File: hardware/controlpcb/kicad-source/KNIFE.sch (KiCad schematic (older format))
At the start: 13 parts, among them P4 WR-TBL_691313710002, U15 74xx08, U16 IFX007T

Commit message: added kicad source
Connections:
- net +3V3: no longer R42.2
- net IS2 renamed KNIFE_IS
- net KNIFE renamed KNIFE_PWM
- new net KNIFE_INH: R42.2
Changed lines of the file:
@@
 IN_KNIFE
-$Comp
-L power-supply:+3V3 #PWR074
-U 1 1 5ECFE999
-P 1900 2000
-F 0 "#PWR074" H 1900 1850 50  0001 C CNN
-F 1 "+3V3" H 1915 2173 50  0000 C CNN
-F 2 "" H 1900 2000 50  0000 C CNN
-F 3 "" H 1900 2000 50  0000 C CNN
-	1    1900 2000
-	1    0    0    -1
-$EndComp
-Wire Wire Line
-	1900 2050 1900 2000
 $Comp
 L IC_logic:74xx08 U15
@@
 EM_STOP
 Text GLabel 2200 4600 0    50   Input ~ 0
-KNIFE
+KNIFE_PWM
 Wire Wire Line
 	2200 4600 2350 4600
@@
 IN_KNIFE
 Text GLabel 3100 6600 2    50   Output ~ 0
-IS2
+KNIFE_IS
 $Comp
 L devices:R_0603 R?
@@
 	1    0    0    1
 $EndComp
+Text GLabel 1900 2050 0    50   Input ~ 0
+KNIFE_INH
 $EndSCHEMATC

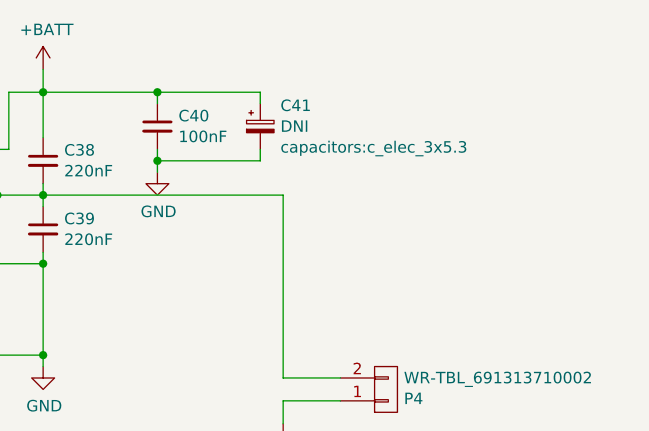
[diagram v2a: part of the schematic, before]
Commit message: added servo connector
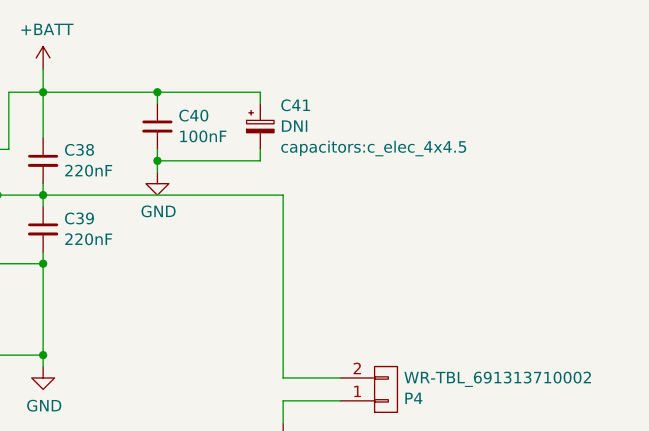
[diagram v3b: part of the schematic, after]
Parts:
- C41: footprint capacitors:c_elec_3x5.3 -> capacitors:c_elec_4x4.5
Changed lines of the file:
@@
 F 0 "C41" H 4988 1691 50  0000 L CNN
 F 1 "DNI" H 4988 1600 50  0000 L CNN
-F 2 "capacitors:c_elec_3x5.3" H 4988 1509 50  0000 L CNN
+F 2 "capacitors:c_elec_4x4.5" H 4988 1509 50  0000 L CNN
 F 3 "" H 4900 1600 50  0000 C CNN
 	1    4900 1600
